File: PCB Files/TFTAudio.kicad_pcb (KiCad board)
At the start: 2 copper layers, 118 x 53.5 mm, 40 parts, among them J1 USB_C_Receptacle_USB2.0_14P, J2 Conn_01x02, J3 Conn_01x14_Socket, J4 Conn_01x06_Socket, J5 Conn_01x12_Pin, Q1 BSS138, Q2 BSS138, Q3 DMG2301L, SW1 SW_SPST, U1 ESP32-WROVER-E, U2 CH340C, U3 MCP73831-2-OT, U4 AP2112K-3.3

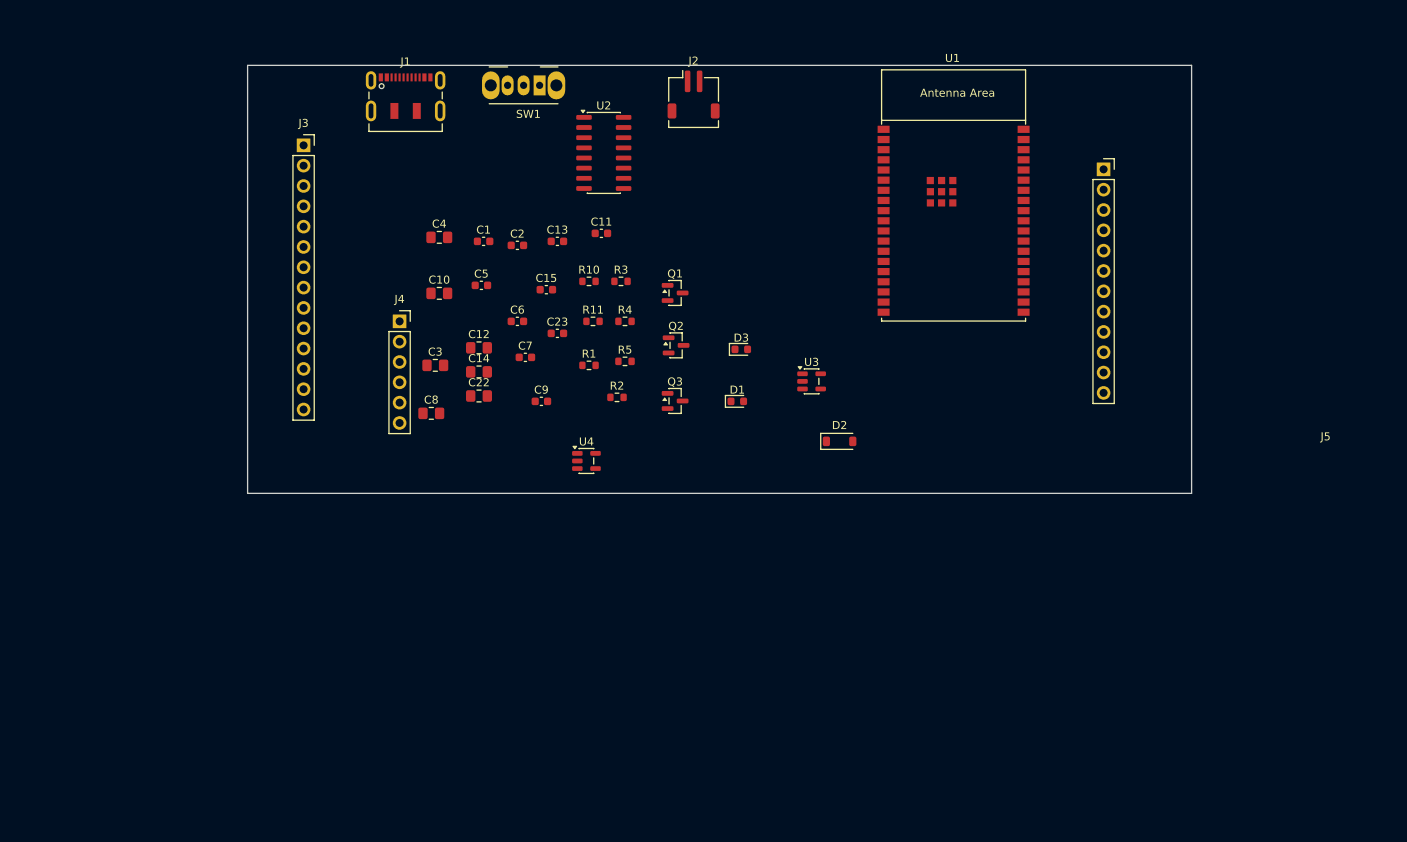
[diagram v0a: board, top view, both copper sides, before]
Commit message: uodated PCB files - added PCM5102
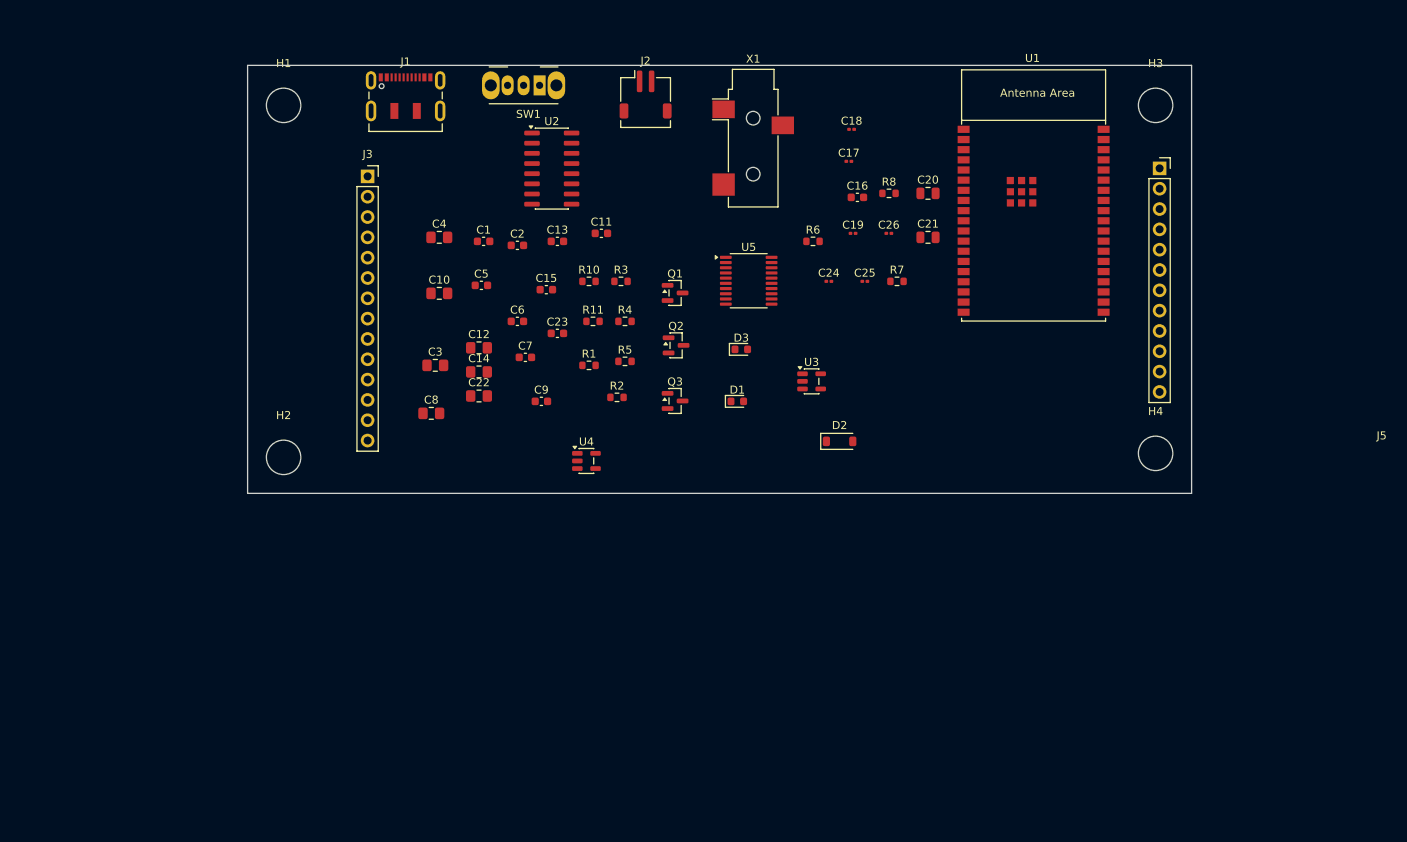
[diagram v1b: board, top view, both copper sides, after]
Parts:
- removed J4: Conn_01x06_Socket, Connector_PinSocket_2.54mm:PinSocket_1x06_P2.54mm_Vertical
- added C16: 2.2nF, Capacitor_SMD:C_0603_1608Metric, F.Cu at (89.2, 35.0)
- added C17: 2.2nF, Capacitor_SMD:C_0201_0603Metric, F.Cu at (88.2, 30.5)
- added C18: 100nF, Capacitor_SMD:C_0201_0603Metric, F.Cu at (88.5, 26.5)
- added C19: 100nF, Capacitor_SMD:C_0201_0603Metric, F.Cu at (88.7, 39.5)
- added C20: 10uF, Capacitor_SMD:C_0805_2012Metric, F.Cu at (98.0, 34.5)
- added C21: 2.2uF, Capacitor_SMD:C_0805_2012Metric, F.Cu at (98.0, 40.0)
- added C24: 2.2uF, Capacitor_SMD:C_0201_0603Metric, F.Cu at (85.7, 45.5)
- added C25: 100nF, Capacitor_SMD:C_0201_0603Metric, F.Cu at (90.2, 45.5)
- added C26: 100nF, Capacitor_SMD:C_0201_0603Metric, F.Cu at (93.2, 39.5)
- added H1: MountingHole, MountingHole:MountingHole_4.3mm_M4, F.Cu at (17.5, 23.5)
- added H2: MountingHole, MountingHole:MountingHole_4.3mm_M4, F.Cu at (17.5, 67.5)
- added H3: MountingHole, MountingHole:MountingHole_4.3mm_M4, F.Cu at (126.5, 23.5)
- added H4: MountingHole, MountingHole:MountingHole_4.3mm_M4, F.Cu at (126.5, 67.0)
- added R6: 470R, Resistor_SMD:R_0603_1608Metric, F.Cu at (83.7, 40.5)
- added R7: 470R, Resistor_SMD:R_0603_1608Metric, F.Cu at (94.2, 45.5)
- added R8: 10K, Resistor_SMD:R_0603_1608Metric, F.Cu at (93.2, 34.5)
- added U5: PCM5102A, Package_SO:TSSOP-20_4.4x6.5mm_P0.65mm, F.Cu at (75.6, 45.4)
- added X1: STEREO_AUDIO_JACK, Connector_Audio:Jack_3.5mm_CUI_SJ-3523-SMT_Horizontal, F.Cu at (76.2, 27.6)
- moved U1 10.0 mm to (111.2, 34.8)
- moved J3 8.89 mm to (28.0, 32.4)
- moved J5 7.00 mm to (127.0, 31.4)
- moved U2 6.79 mm to (51.0, 31.4)
- moved J2 6.00 mm to (62.8, 22.1)

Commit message: Mark R Commit - PCB help
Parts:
- added R9: 100k, Resistor_SMD:R_0603_1608Metric, F.Cu at (35.8, 32.2)
- C10, C14, C22, C3, C4, C8: footprint Capacitor_SMD:C_0805_2012Metric_Pad1.18x1.45mm_HandSolder -> Capacitor_SMD:C_0603_1608Metric
- C17, C18, C19, C24, C25, C26: footprint Capacitor_SMD:C_0201_0603Metric -> Capacitor_SMD:C_0603_1608Metric
- C20, C21: footprint Capacitor_SMD:C_0805_2012Metric -> Capacitor_SMD:C_0603_1608Metric
- D1: value LED -> Charge
- H1, H2, H3, H4: footprint MountingHole:MountingHole_4.3mm_M4 -> MountingHole:MountingHole_3.2mm_M3_ISO14580
- J2: value Conn_01x02 -> Lipo 1S
- J3: value Conn_01x14_Socket -> Display
- J5: value Conn_01x12_Pin -> expansion
- moved U1 79.3 mm to (37.0, 62.6), turned to 180 degrees
- moved U2 71.4 mm to (-12.5, 64.0)
- moved C16 69.5 mm to (125.0, 94.5)
- moved C17 69.5 mm to (124.0, 90.0)
- moved C18 69.5 mm to (124.3, 86.0)
- moved C20 69.5 mm to (133.9, 94.0)
- moved C21 69.5 mm to (133.9, 99.5)
- moved C25 69.5 mm to (126.0, 105.0)
- moved R7 69.5 mm to (130.0, 105.0)
- moved R8 69.5 mm to (129.0, 94.0)
- moved C19 69.5 mm to (124.5, 99.0)
- moved C26 69.5 mm to (129.0, 99.0)
- moved D2 66.6 mm to (31.6, 28.6)
- moved R6 64.5 mm to (133.0, 82.0)
- moved U5 57.1 mm to (130.0, 63.0)
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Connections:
- net Net-(D2-K) renamed /SWIN
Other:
- board size 118 x 53.5 mm -> 108 x 60.9 mm

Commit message: pcb - finished draft 1.0
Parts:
- removed C10: 10u, Capacitor_SMD:C_0603_1608Metric
- removed C11, C13: 100n, Capacitor_SMD:C_0603_1608Metric
- removed C12: 10u, Capacitor_SMD:C_0805_2012Metric_Pad1.18x1.45mm_HandSolder
- removed J1: USB_C_Receptacle_USB2.0_14P, Connector_USB:USB_C_Receptacle_JAE_DX07S016JA1R1500
- removed X1: STEREO_AUDIO_JACK, Connector_Audio:Jack_3.5mm_CUI_SJ-3523-SMT_Horizontal
- added J4: AudioJack3, Connector_Audio:Jack_3.5mm_CUI_SJ1-3523N_Horizontal, F.Cu at (101.8, 23.1)
- added J6: USB_C_Receptacle_USB2.0_14P, Connector_USB:USB_C_Receptacle_HRO_TYPE-C-31-M-12, F.Cu at (33.7, 23.5)
- moved C8 109.2 mm to (115.1, 35.4), turned to -90 degrees
- moved C9 101.2 mm to (115.1, 32.4), turned to 90 degrees
- moved R5 90.7 mm to (26.3, 23.2), turned to -90 degrees
- moved R4 89.0 mm to (26.3, 20.1), turned to 90 degrees
- moved Q2 79.2 mm to (35.4, 32.7), turned to -90 degrees
- moved C6 78.7 mm to (41.5, 23.1), turned to -90 degrees
- moved C14 77.6 mm to (19.2, 34.2), turned to -90 degrees
- moved C7 76.4 mm to (45.4, 29.7)
- moved R11 75.7 mm to (26.5, 32.8), turned to 90 degrees
- moved C15 74.2 mm to (19.2, 31.2), turned to 90 degrees
- moved C1 71.5 mm to (41.4, 20.0), turned to 90 degrees
- moved R7 71.0 mm to (95.5, 43.0), turned to 90 degrees
- moved C21 70.0 mm to (85.6, 48.8), turned to 90 degrees
- moved Q1 69.1 mm to (35.4, 37.3), turned to 90 degrees
- moved C25 64.7 mm to (98.1, 46.6), turned to 90 degrees
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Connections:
- net Net-(D3-A) renamed /REGIN
- J5 pad 10: /GPI35 -> /GPI36
- J5 pad 11: /GPI36 -> +3.3V
- J5 pad 12: /GPI39 -> GND
- J5 pad 2: +5V -> GND
- J5 pad 3: GND -> /CTP_SDA
- J5 pad 4: /CTP_SDA -> /CTP_SCL
- J5 pad 5: /CTP_SCL -> /SD_CS
- J5 pad 6: +3.3V -> /GPIO4
- J5 pad 7: GND -> /GPIO15
- J5 pad 8: /GPIO32 -> /GPIO19
- J5 pad 9: /GPI34 -> /GPI35
- U1 pad 11: /SD_CS -> /CTP_RST
- U1 pad 23: /LCD_CS -> /GPIO15
- U1 pad 26: /CTP_RST -> /GPIO4
- U1 pad 29: /CTP_INT -> /SD_CS
- U1 pad 31: /MISO -> /GPIO19
- U1 pad 5: /GPI39 -> /CTP_INT
- U1 pad 6: /GPI34 -> /MISO
- U1 pad 8: /GPIO32 -> /LCD_RST
- U1 pad 9: /LCD_RST -> /LCD_CS
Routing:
- net GND: track 0.00 -> 486.7 mm, vias 0 -> 24
- net +3.3V: track 0.00 -> 228.0 mm, vias 0 -> 8
- net /CTP_SDA: track 0.00 -> 147.9 mm, vias 0 -> 4
- net /SD_CS: track 0.00 -> 137.4 mm, vias 0 -> 5
- net /CTP_SCL: track 0.00 -> 137.0 mm, vias 0 -> 4
- net +5V: track 0.00 -> 125.3 mm, vias 0 -> 5
- net /GPIO19: track 0.00 -> 103.3 mm, vias 0 -> 4
- net /GPIO4: track 0.00 -> 98.1 mm, vias 0 -> 3
- net /GPIO15: track 0.00 -> 96.3 mm
- net /GPI36: track 0.00 -> 78.7 mm
- net /GPI35: track 0.00 -> 76.9 mm
- net /EN: track 0.00 -> 66.4 mm, vias 0 -> 2
- net /RX: track 0.00 -> 58.8 mm, vias 0 -> 2
- net /LRCK: track 0.00 -> 52.0 mm, vias 0 -> 2
- net /DATA: track 0.00 -> 50.8 mm
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- added copper zone on B.Cu, net GND
- added copper zone on F.Cu, net GND
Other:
- outline, holes or cut-outs redrawn

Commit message: PCB Draft 3
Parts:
- added SW2: RESET, Button_Switch_THT:SW_Tactile_SKHH_Angled, F.Cu at (59.1, 75.6)
- D1, D3: footprint LED_SMD:LED_0603_1608Metric -> LED_SMD:LED_0805_2012Metric
- U1: footprint Espressif:ESP32-WROVER-E -> PCM_Espressif:ESP32-WROVER-E
- moved J4 1.50 mm to (101.8, 24.6)
- moved R10 1.00 mm to (64.2, 24.0), turned to 180 degrees
- moved J2 0.92 mm to (75.6, 22.1)
- moved U1 0.72 mm to (36.6, 62.0)
- moved J5 0.47 mm to (118.5, 34.0)
- moved C9 0.47 mm to (114.6, 32.4)
- moved C8 0.47 mm to (114.6, 35.4)
- moved D3 0.43 mm to (64.1, 19.5), turned to 0 degrees
- moved D1 0.41 mm to (82.1, 19.5), turned to 0 degrees
- moved J6 0.32 mm to (33.9, 23.8)
- moved R5 0.20 mm to (26.3, 23.0)
- moved R1 0.13 mm to (82.0, 22.9), turned to 0 degrees
- moved C6 0.11 mm to (41.4, 23.1)
- moved SW1 0.11 mm to (58.2, 20.9)
- moved R4 0.08 mm to (26.3, 20.0)
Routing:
- net /CTP_SDA: track 147.9 -> 125.3 mm
- net /CTP_RST: track 47.6 -> 69.2 mm, vias 2 -> 4
- net /EN: track 66.4 -> 85.3 mm
- net +3.3V: track 228.0 -> 244.4 mm, vias 8 -> 10
- net /SD_CS: track 137.4 -> 126.6 mm, vias 5 -> 0
- net /GPIO15: track 96.3 -> 106.2 mm, vias 0 -> 2
- net Net-(D3-K): track 3.72 -> 12.1 mm, vias 0 -> 2
- net /MISO: track 38.2 -> 46.4 mm, vias 2 -> 1
- net /MOSI: track 32.9 -> 40.8 mm
- net /GPIO19: track 103.3 -> 95.4 mm, vias 4 -> 2
- net /SWIN: track 35.2 -> 27.4 mm
- net /BCK: track 50.5 -> 57.9 mm, vias 0 -> 2
- net Net-(U3-STAT): track 14.2 -> 20.6 mm, vias 0 -> 2
- net Net-(C17-Pad2): track 26.0 -> 20.1 mm, vias 1 -> 0
- net Net-(J2-Pin_1): track 26.5 -> 32.2 mm, vias 0 -> 2
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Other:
- outline, holes or cut-outs redrawn

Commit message: PCB draft 4
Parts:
- moved J6 1.13 mm to (34.0, 22.6), turned to 180 degrees
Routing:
- net /CTP_RST: track 69.2 -> 35.2 mm, vias 4 -> 2
- net GND: track 484.6 -> 463.2 mm, vias 4 -> 10
- net +3.3V: track 244.4 -> 263.0 mm, vias 10 -> 6
- net +5V: track 128.9 -> 116.0 mm, vias 4 -> 2
- net /EN: track 85.3 -> 74.1 mm
- net Net-(U5-OUTR): track 13.4 -> 23.5 mm
- net /DATA: track 51.8 -> 59.7 mm, vias 0 -> 4
- net /SCK: track 30.1 -> 22.5 mm
- net Net-(D3-K): track 12.1 -> 5.26 mm, vias 2 -> 0
- net /BCK: track 57.9 -> 51.1 mm, vias 2 -> 0
- net /MISO: track 46.4 -> 39.8 mm
- net Net-(U2-UD-): track 21.4 -> 15.5 mm
- net /CTP_SCL: track 135.9 -> 130.3 mm, vias 3 -> 4
- net Net-(U3-STAT): track 20.6 -> 15.4 mm, vias 2 -> 0
- net Net-(C17-Pad2): track 20.1 -> 24.8 mm, vias 0 -> 1
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
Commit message: PCB Draft 5
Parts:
- SW2: footprint Button_Switch_THT:SW_Tactile_SKHH_Angled -> Button_Switch_SMD:SW_SPST_EVQP7C
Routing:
- net +3.3V: track 263.0 -> 239.2 mm, vias 6 -> 7
- net /SD_CS: track 127.1 -> 146.3 mm, vias 0 -> 3
- net Net-(U5-OUTR): track 23.5 -> 13.9 mm
- net Net-(Q1-G): track 29.2 -> 20.5 mm
- net /CTP_SDA: track 122.2 -> 130.9 mm, vias 3 -> 4
- net /EN: track 74.1 -> 82.3 mm
- net +5V: track 116.0 -> 123.9 mm, vias 2 -> 4
- net GND: track 463.2 -> 455.4 mm, vias 10 -> 5
- net /CTP_SCL: track 130.3 -> 136.7 mm, vias 4 -> 2
- net Net-(U5-OUTL): track 12.8 -> 18.1 mm
- net Net-(C17-Pad2): track 24.8 -> 20.2 mm, vias 1 -> 0
- net Net-(Q1-S): track 19.9 -> 15.7 mm
- net /REGIN: track 48.8 -> 52.3 mm
- net /LED: track 40.2 -> 43.5 mm
- net /DATA: track 59.7 -> 56.5 mm
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
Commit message: PCB Final Draft
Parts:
- moved J2 60.9 mm to (115.5, 68.1), turned to -90 degrees
- moved R1 12.9 mm to (69.1, 23.0), turned to 90 degrees
- moved D1 12.1 mm to (70.0, 20.0)
- moved J5 2.20 mm to (116.4, 33.6)
- moved C9 2.15 mm to (112.5, 32.3)
- moved C8 2.11 mm to (112.5, 35.5)
- moved R10 1.47 mm to (63.1, 23.0), turned to -90 degrees
- moved D3 0.47 mm to (64.0, 20.0)
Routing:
- net Net-(J2-Pin_1): track 27.6 -> 80.0 mm, vias 0 -> 2
- net GND: track 455.4 -> 478.8 mm, vias 5 -> 6
- net /GPIO4: track 97.1 -> 119.8 mm, vias 0 -> 4
- net /GPIO15: track 110.2 -> 94.3 mm, vias 2 -> 0
- net /GPIO19: track 97.6 -> 108.5 mm
- net /MISO: track 39.9 -> 49.4 mm
- net /RX: track 55.4 -> 46.1 mm
- net /LRCK: track 50.7 -> 59.8 mm
- net /CTP_SDA: track 130.9 -> 123.3 mm
- net /CTP_SCL: track 136.7 -> 130.1 mm, vias 2 -> 1
- net Net-(U5-OUTL): track 18.1 -> 11.6 mm
- net /LED: track 43.5 -> 37.1 mm, vias 2 -> 1
- net /CTP_INT: track 39.2 -> 33.1 mm, vias 1 -> 2
- net /BCK: track 50.6 -> 56.5 mm, vias 0 -> 2
- net /EN: track 82.3 -> 77.1 mm, vias 2 -> 3
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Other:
- outline, holes or cut-outs redrawn
- board text added: "Alan Trundle ESP32 WROVER Audio DAC Board V1.0 8MB Flash / 8MB PSRAM 14/12/2025"

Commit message: Submitted PCB
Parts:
- C1, C15, C2, C23, C5, C7, C9: value 100n -> 100nF
- C14, C22, C3, C4, C8: value 10u -> 10uF
- C6: value 1u -> 10uF
- Q1, Q2: value BSS138 -> AO3400A
- Q3: value DMG2301L -> AO3401A
- R10: value 220 -> 220R
- R11: value 10k -> 10K
- R2: value 2k -> 2.2k
- R9: value 100k -> 100K
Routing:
- net +3.3V: track 236.5 -> 239.4 mm
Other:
- outline, holes or cut-outs redrawn
- board text added: "+"
- board text added: "-"
- board text added: "CHG"
- board text added: "PWR"
